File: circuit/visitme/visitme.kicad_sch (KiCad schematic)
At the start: 16 parts, among them J5V1 Conn_01x01_Female, Q1 BC237

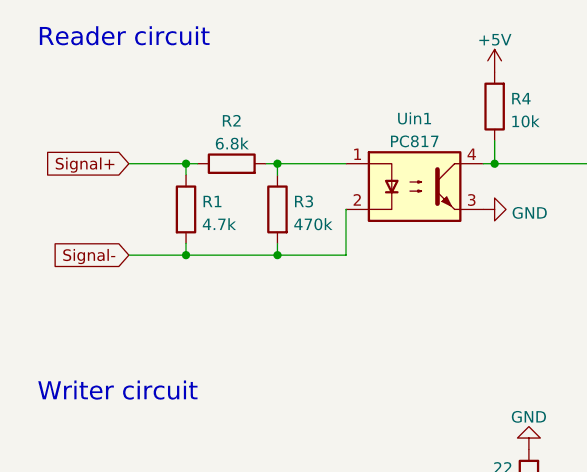
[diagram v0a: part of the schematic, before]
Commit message: removed redundant 470k
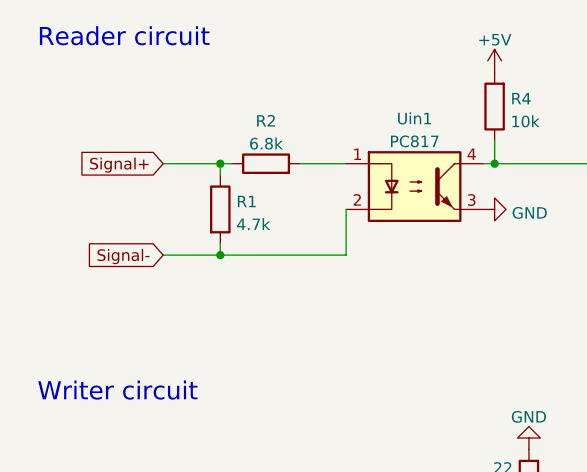
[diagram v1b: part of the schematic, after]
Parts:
- removed R3: 470k, Resistor_THT:R_Axial_DIN0204_L3.6mm_D1.6mm_P7.62mm_Horizontal, symbol Device:R
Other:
- moved on the sheet: R1, R2
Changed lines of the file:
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@@
 (kicad_sch (version 20230121) (generator eeschema)
   (paper "A4")
-  (junction (at 66.04 50.8) (diameter 0) (color 0 0 0 0)
-  )
-  (junction (at 66.04 40.64) (diameter 0) (color 0 0 0 0)
-  )
-  (junction (at 76.2 50.8) (diameter 0) (color 0 0 0 0)
-  )
-  (junction (at 76.2 40.64) (diameter 0) (color 0 0 0 0)
+  (junction (at 69.85 50.8) (diameter 0) (color 0 0 0 0)
+  )
+  (junction (at 69.85 40.64) (diameter 0) (color 0 0 0 0)
   )
   (junction (at 100.33 40.64) (diameter 0) (color 0 0 0 0)
@@
     (stroke (width 0) (type default))
   )
-  (wire (pts (xy 76.2 50.8) (xy 66.04 50.8))
-    (stroke (width 0) (type default))
-  )
   (wire (pts (xy 83.82 45.72) (xy 83.82 50.8))
     (stroke (width 0) (type default))
@@
     (stroke (width 0) (type default))
   )
-  (wire (pts (xy 59.69 40.64) (xy 66.04 40.64))
-    (stroke (width 0) (type default))
-  )
-  (wire (pts (xy 59.69 50.8) (xy 66.04 50.8))
+  (wire (pts (xy 63.5 40.64) (xy 69.85 40.64))
+    (stroke (width 0) (type default))
+  )
+  (wire (pts (xy 63.5 50.8) (xy 69.85 50.8))
     (stroke (width 0) (type default))
   )
@@
     (stroke (width 0) (type default))
   )
-  (wire (pts (xy 67.31 40.64) (xy 66.04 40.64))
-    (stroke (width 0) (type default))
-  )
-  (wire (pts (xy 66.04 40.64) (xy 66.04 41.91))
+  (wire (pts (xy 71.12 40.64) (xy 69.85 40.64))
+    (stroke (width 0) (type default))
+  )
+  (wire (pts (xy 69.85 40.64) (xy 69.85 41.91))
     (stroke (width 0) (type default))
   )
@@
     (stroke (width 0) (type default))
   )
-  (wire (pts (xy 76.2 49.53) (xy 76.2 50.8))
-    (stroke (width 0) (type default))
-  )
-  (wire (pts (xy 74.93 40.64) (xy 76.2 40.64))
-    (stroke (width 0) (type default))
-  )
-  (wire (pts (xy 76.2 40.64) (xy 76.2 41.91))
+  (wire (pts (xy 78.74 40.64) (xy 83.82 40.64))
     (stroke (width 0) (type default))
   )
@@
     (stroke (width 0) (type default))
   )
-  (wire (pts (xy 76.2 40.64) (xy 83.82 40.64))
-    (stroke (width 0) (type default))
-  )
   (wire (pts (xy 63.5 80.01) (xy 83.82 80.01))
     (stroke (width 0) (type default))
@@
     (stroke (width 0) (type default))
   )
-  (wire (pts (xy 66.04 50.8) (xy 66.04 49.53))
+  (wire (pts (xy 69.85 50.8) (xy 69.85 49.53))
     (stroke (width 0) (type default))
   )
@@
     (stroke (width 0) (type default))
   )
-  (wire (pts (xy 83.82 50.8) (xy 76.2 50.8))
+  (wire (pts (xy 69.85 50.8) (xy 83.82 50.8))
     (stroke (width 0) (type default))
   )
@@
     (effects (font (size 2 2)) (justify left bottom))
   )
-  (global_label "Signal+" (shape input) (at 59.69 40.64 180) (fields_autoplaced)
-    (effects (font (size 1.27 1.27)) (justify right))
-    (property "Intersheetrefs" "${INTERSHEET_REFS}" (at 49.7779 40.7194 0)
-      (effects (font (size 1.27 1.27)) (justify right) hide)
-    )
-  )
-  (global_label "Signal-" (shape input) (at 59.69 50.8 180) (fields_autoplaced)
-    (effects (font (size 1.27 1.27)) (justify right))
-    (property "Intersheetrefs" "${INTERSHEET_REFS}" (at 49.7779 50.7206 0)
+  (global_label "Signal+" (shape input) (at 63.5 40.64 180) (fields_autoplaced)
+    (effects (font (size 1.27 1.27)) (justify right))
+    (property "Intersheetrefs" "${INTERSHEET_REFS}" (at 53.5879 40.7194 0)
+      (effects (font (size 1.27 1.27)) (justify right) hide)
+    )
+  )
+  (global_label "Signal-" (shape input) (at 63.5 50.8 180) (fields_autoplaced)
+    (effects (font (size 1.27 1.27)) (justify right))
+    (property "Intersheetrefs" "${INTERSHEET_REFS}" (at 53.5879 50.7206 0)
       (effects (font (size 1.27 1.27)) (justify right) hide)
     )
@@
     )
   )
-  (symbol (lib_id "Device:R") (at 66.04 45.72 0) (unit 1)
+  (symbol (lib_id "Device:R") (at 69.85 45.72 0) (unit 1)
     (in_bom yes) (on_board yes) (dnp no)
-    (property "Reference" "R1" (at 67.818 44.8853 0)
-      (effects (font (size 1.27 1.27)) (justify left))
-    )
-    (property "Value" "4.7k" (at 67.818 47.4222 0)
-      (effects (font (size 1.27 1.27)) (justify left))
-    )
-    (property "Footprint" "Resistor_THT:R_Axial_DIN0204_L3.6mm_D1.6mm_P7.62mm_Horizontal" (at 64.262 45.72 90)
-      (effects (font (size 1.27 1.27)) hide)
-    )
-    (property "Datasheet" "~" (at 66.04 45.72 0)
+    (property "Reference" "R1" (at 71.628 44.8853 0)
+      (effects (font (size 1.27 1.27)) (justify left))
+    )
+    (property "Value" "4.7k" (at 71.628 47.4222 0)
+      (effects (font (size 1.27 1.27)) (justify left))
+    )
+    (property "Footprint" "Resistor_THT:R_Axial_DIN0204_L3.6mm_D1.6mm_P7.62mm_Horizontal" (at 68.072 45.72 90)
+      (effects (font (size 1.27 1.27)) hide)
+    )
+    (property "Datasheet" "~" (at 69.85 45.72 0)
       (effects (font (size 1.27 1.27)) hide)
     )
@@
         (path "/8f5fa9db-9322-46a0-afd1-ee59d57422cc"
           (reference "JS-1") (unit 1)
-        )
-      )
-    )
-  )
-  (symbol (lib_id "Device:R") (at 76.2 45.72 0) (mirror y) (unit 1)
-    (in_bom yes) (on_board yes) (dnp no) (fields_autoplaced)
-    (property "Reference" "R3" (at 77.978 44.8853 0)
-      (effects (font (size 1.27 1.27)) (justify right))
-    )
-    (property "Value" "470k" (at 77.978 47.4222 0)
-      (effects (font (size 1.27 1.27)) (justify right))
-    )
-    (property "Footprint" "Resistor_THT:R_Axial_DIN0204_L3.6mm_D1.6mm_P7.62mm_Horizontal" (at 77.978 45.72 90)
-      (effects (font (size 1.27 1.27)) hide)
-    )
-    (property "Datasheet" "~" (at 76.2 45.72 0)
-      (effects (font (size 1.27 1.27)) hide)
-    )
-    (pin "1")
-    (pin "2")
-    (instances
-      (project "visitme"
-        (path "/8f5fa9db-9322-46a0-afd1-ee59d57422cc"
-          (reference "R3") (unit 1)
         )
       )
@@
     )
   )
-  (symbol (lib_id "Device:R") (at 71.12 40.64 90) (unit 1)
-    (in_bom yes) (on_board yes) (dnp no) (fields_autoplaced)
-    (property "Reference" "R2" (at 71.12 35.9242 90)
-      (effects (font (size 1.27 1.27)))
-    )
-    (property "Value" "6.8k" (at 71.12 38.4611 90)
-      (effects (font (size 1.27 1.27)))
-    )
-    (property "Footprint" "Resistor_THT:R_Axial_DIN0204_L3.6mm_D1.6mm_P7.62mm_Horizontal" (at 71.12 42.418 90)
-      (effects (font (size 1.27 1.27)) hide)
-    )
-    (property "Datasheet" "~" (at 71.12 40.64 0)
-      (effects (font (size 1.27 1.27)) hide)
-    )
+  (symbol (lib_id "Device:R") (at 74.93 40.64 90) (unit 1)
+    (in_bom yes) (on_board yes) (dnp no) (fields_autoplaced)
+    (property "Reference" "R2" (at 74.93 35.9242 90)
+      (effects (font (size 1.27 1.27)))
+    )
+    (property "Value" "6.8k" (at 74.93 38.4611 90)
+      (effects (font (size 1.27 1.27)))
+    )
+    (property "Footprint" "Resistor_THT:R_Axial_DIN0204_L3.6mm_D1.6mm_P7.62mm_Horizontal" (at 74.93 42.418 90)
+      (effects (font (size 1.27 1.27)) hide)
+    )
+    (property "Datasheet" "~" (at 74.93 40.64 0)
+      (effects (font (size 1.27 1.27)) hide)
+    )

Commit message: further board refinement
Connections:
- net +5V: now also Q1.1 (C); no longer Q1.3 (E)
- net at Uout1.1: now also Q1.3 (E); no longer Q1.1 (C)
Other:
- company: (none) -> undefspace
- title: (none) -> Sebaschan Circuit
- moved on the sheet: J5V1, JDI1, JDO1, JGND1, JS+1, JS-1, Q1, R1, R2, R4, R5, R6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
